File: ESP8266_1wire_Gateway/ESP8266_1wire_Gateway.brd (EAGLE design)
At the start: 44 x 44 mm, 72 parts, among them IC1 5V, IC2 3.3V, IC3 DS2482-100S, IC4 DS18B20, Q1 BSS84, Q2 BSS138, Q3 BSS138

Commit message: .
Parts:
- removed FLASH_SW: DTSM-3, mechanics:DTSM-3
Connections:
- net GND: no longer FLASH_SW.2
- net N$10: no longer FLASH_SW.1
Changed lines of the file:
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@@
 <element name="R14" library="resistor" package="R0805" value="4k7" x="11.1125" y="31.4325" rot="MR90"/>
 <element name="R13" library="resistor" package="R0805" value="4k7" x="14.2875" y="18.0975" rot="MR90"/>
-<element name="FLASH_SW" library="mechanics" package="DTSM-3" value="DTSM-3" x="26.7335" y="6.985" smashed="yes">
-<attribute name="NAME" x="24.1935" y="8.89" size="1.016" layer="25" ratio="14"/>
-</element>
 <element name="U$1" library="ohw-logo" package="OSHW_FILLX100_NOTEXT" value="" x="43.4275" y="34.5375" rot="MR0"/>
 <element name="IC2" library="SparkFun-PowerIC" package="SOT223" value="3.3V" x="21.082" y="18.7325" smashed="yes" rot="R180">
@@
 <contactref element="RESET" pad="1"/>
 <contactref element="C3" pad="2"/>
-<contactref element="FLASH_SW" pad="2"/>
 <contactref element="C6" pad="2"/>
 <contactref element="IC2" pad="1"/>
@@
 <wire x1="23.1762" y1="3.175" x2="20.32" y2="9.205" width="0" layer="19" extent="1-1"/>
 <wire x1="20.0025" y1="1.425" x2="23.1762" y2="3.175" width="0" layer="19" extent="1-1"/>
-<wire x1="30.2273" y1="6.985" x2="23.2397" y2="10.668" width="0" layer="19" extent="1-1"/>
-<wire x1="41.91" y1="9.525" x2="30.2273" y2="6.985" width="0" layer="19" extent="1-1"/>
-<wire x1="38.1" y1="7.62" x2="20.0025" y2="1.425" width="0" layer="19" extent="1-1"/>
+<wire x1="38.1" y1="7.62" x2="23.2397" y2="10.668" width="0" layer="19" extent="1-1"/>
+<wire x1="41.91" y1="9.525" x2="38.1" y2="7.62" width="0" layer="19" extent="1-1"/>
 </signal>
 <signal name="N$1">
@@
 <signal name="N$10">
 <contactref element="FLASH" pad="2"/>
-<contactref element="FLASH_SW" pad="1"/>
 <contactref element="R12" pad="1"/>
-<wire x1="13.0175" y1="9.21" x2="23.2397" y2="6.985" width="0" layer="19" extent="1-1"/>
-<wire x1="38.1" y1="10.16" x2="13.0175" y2="9.21" width="0" layer="19" extent="1-1"/>
+<wire x1="13.0175" y1="9.21" x2="38.1" y2="10.16" width="0" layer="19" extent="1-1"/>
 </signal>
 </signals>

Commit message: v0.9
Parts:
- removed CLR: (no value), my:1X02
- removed G12, G13: LSP10, my:LSP10
- added 1W1, 1W2: (no value), my:1X03
- added G4, G5: LSP10, my:LSP10
- added HSPI: (no value), my:1X04
- RST: value GND -> RST
- moved R1 33.5 mm to (36.2, 8.57)
- moved U$1 33.3 mm to (43.1, 1.20)
- moved U$2 33.3 mm to (40.3, 1.20)
- moved R3 32.2 mm to (28.6, 8.57)
- moved PF1 26.4 mm to (31.8, 25.7), turned to 0 degrees
- moved PRG 26.4 mm to (35.9, 31.4), turned to 180 degrees
- moved R14 26.0 mm to (23.5, 8.57), turned to 270 degrees
- moved R12 24.8 mm to (37.8, 8.26)
- moved R10 24.6 mm to (31.1, 8.57)
- moved C4 24.1 mm to (7.62, 36.5)
- moved SJ4 21.8 mm to (11.7, 32.1)
- moved SJ5 20.5 mm to (14.3, 32.1)
- moved R11 19.6 mm to (33.7, 8.57)
- moved R7 18.7 mm to (26.0, 8.57)
- moved SJ3 18.1 mm to (17.1, 32.1), turned to 90 degrees
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- renumbered GND8 to RST
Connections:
- net CSN renamed GPIO15
- removed net GPIO0: G0.1, MDL1.12, R12.2, R5.1
- removed net GPIO2: G2.1, MDL1.11, R4.1, SJ3.1
- new net 1WDIR: G0.1, MDL1.12, R12.2, R5.1, SJ3.1
- new net GPIO5: G5.1, MDL1.14, R8.1
- new net HCS0: HSPI.4, MDL1.17
- new net HMISO: HSPI.3, MDL1.18
- new net HMOSI: HSPI.2, MDL1.21
- new net HSCLK: HSPI.1, MDL1.22
- net 1W_ESD: now also 1W1.2, 1W2.2
- net GND: no longer RST.1
- net GND_ESD: now also 1W1.3, 1W2.3
- net LED_OPT: now also G4.1, MDL1.13, R9.1; no longer G12.1, MDL1.6, R8.1
- net RST: now also RST.1
- net RXD: no longer CLR.2
- net SCL1: now also MDL1.6; no longer MDL1.14
- net SDA1: now also MDL1.7; no longer MDL1.13
- net SW_OPT: now also G2.1, MDL1.11, R4.1; no longer G13.1, MDL1.7, R9.1
- net TXD: no longer CLR.1
- net VCC_5V: now also 1W1.1, 1W2.1
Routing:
- net GND: track 0.00 -> 204.1 mm, vias 0 -> 3
- net VCC: track 0.00 -> 128.6 mm, vias 0 -> 2
- net VCC_5V: track 0.00 -> 89.1 mm, vias 0 -> 3
- net 5V_IN: track 0.00 -> 86.9 mm, vias 0 -> 2
- net LED_OPT: track 0.00 -> 86.1 mm, vias 0 -> 3
- net SW_OPT: track 0.00 -> 84.2 mm, vias 0 -> 3
- net 1WDIR: track 0.00 -> 80.2 mm, vias 0 -> 2
- net SCL1: track 0.00 -> 70.3 mm, vias 0 -> 2
- net RST: track 0.00 -> 63.4 mm, vias 0 -> 1
- net SDA2: track 0.00 -> 60.4 mm, vias 0 -> 1
- net GPIO15: track 0.00 -> 59.7 mm
- net N$5: track 0.00 -> 58.7 mm
- net SDA1X: track 0.00 -> 56.3 mm, vias 0 -> 1
- net CH_PD: track 0.00 -> 52.5 mm, vias 0 -> 2
- net GPIO5: track 0.00 -> 47.9 mm, vias 0 -> 2
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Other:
- board text added: "CS0"
- board text added: "EXT"
- board text added: "MISO"
- board text added: "MOSI"
- board text added: "RST"
- board text added: "RXD"
- board text added: "SCLK"
- board text added: "TXD"

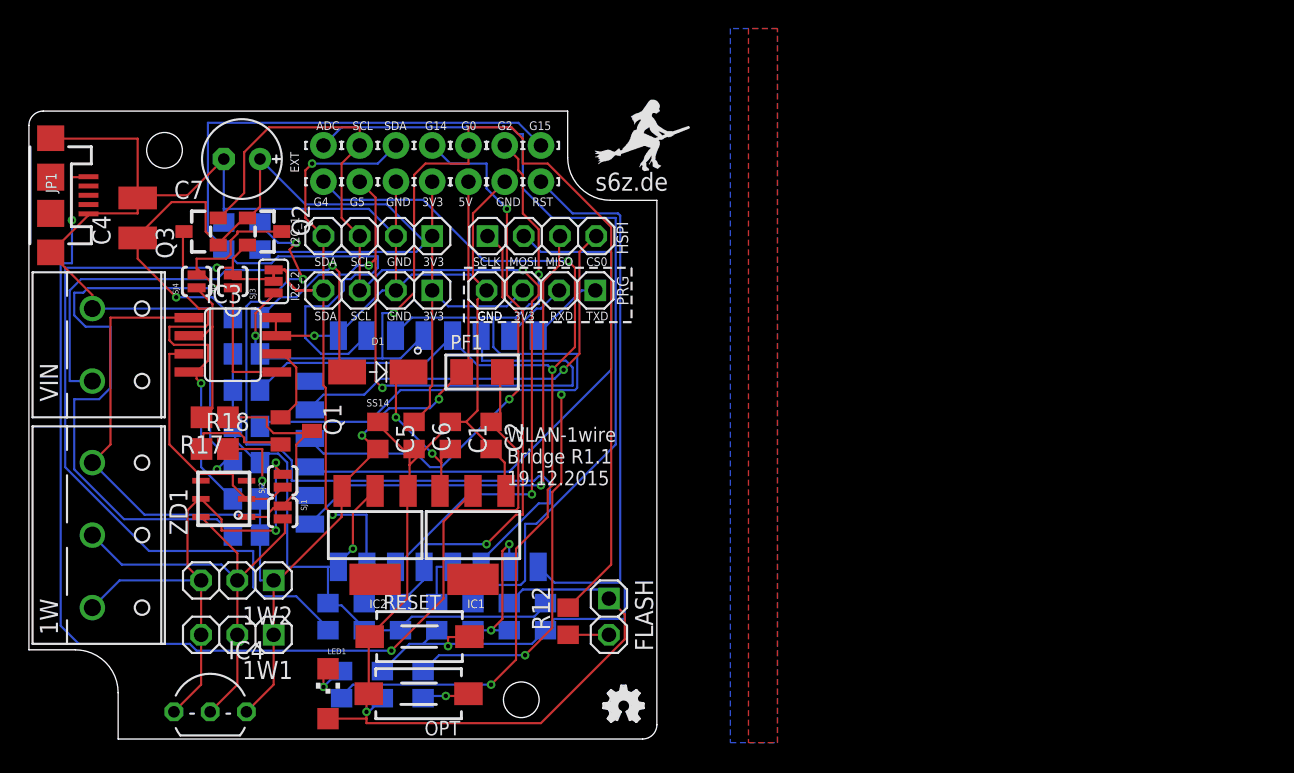
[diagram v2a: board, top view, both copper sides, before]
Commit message: Version 1.2 : ELKO / THT Version 1.3 : tantal / SMD
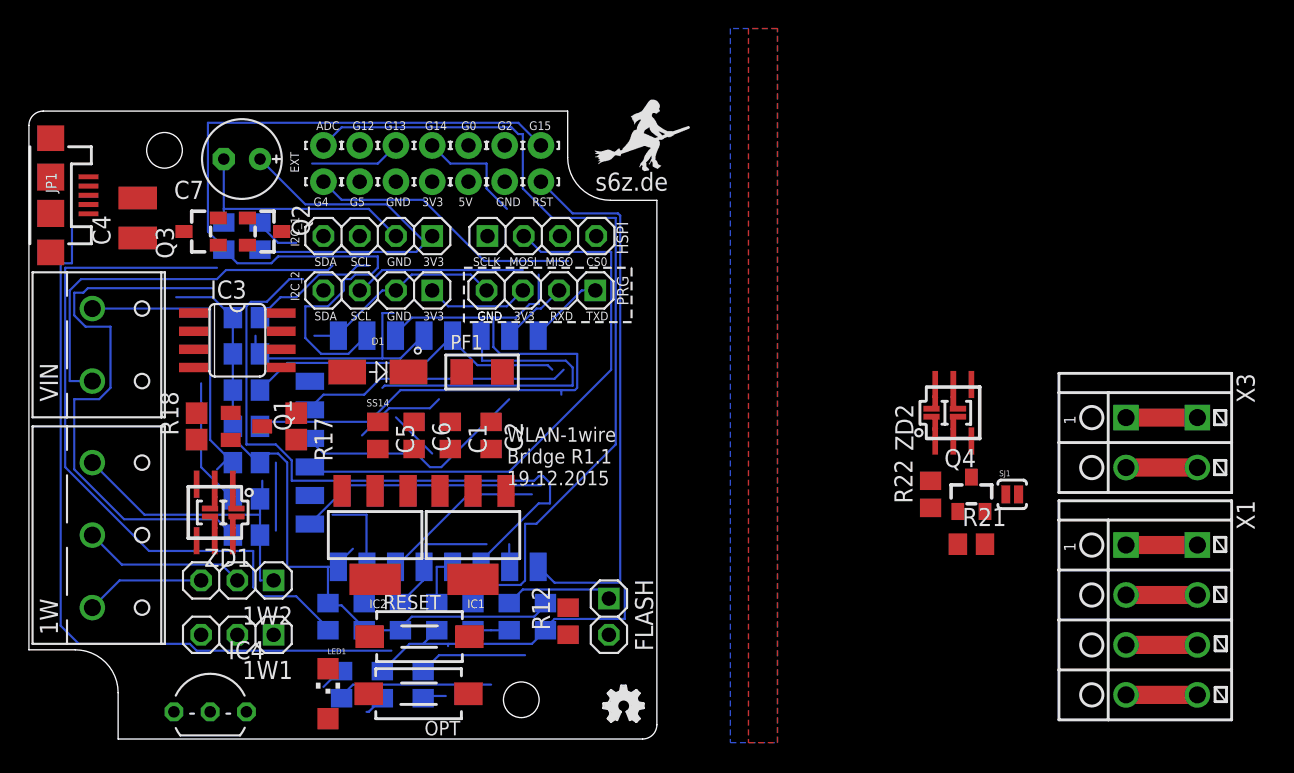
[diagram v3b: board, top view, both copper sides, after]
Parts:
- removed SJ2, SJ4, SJ5: JUMPER-PAD-2-NOYES_SILK, SparkFun-Passives:PAD-JUMPER-2-NO_YES_SILK
- removed SJ3: JUMPER-PAD-3-2OF3_NC_BY_TRACE_SMALL, SparkFun-Passives:PAD-JUMPER-3-2OF3_NC_BY_TRACE_YES_SILK_FULL_BOX
- added Q4: BSS138, my:SOT23
- added R21, R22: 10k, resistor:R0805
- added X1: (no value), my:CON_350-104
- added X3: (no value), my:CON_350-102
- added ZD2: DS9503_BYPASS_JP, my:TSOC6_BYPASS_J
- ZD1: value DS9503P -> DS9503_BYPASS_JP; device 1wire:TSOC6 -> my:TSOC6_BYPASS_J
- moved SJ1 51.1 mm to (68.9, 17.1), turned to 0 degrees
- moved R17 5.75 mm to (18.7, 21.9), turned to 270 degrees
- moved Q1 3.51 mm to (15.2, 21.9)
- moved R18 2.03 mm to (11.7, 21.9), turned to 90 degrees
- moved ZD1 1.14 mm to (13.0, 15.9), turned to 180 degrees
- moved IC3 0.45 mm to (14.6, 27.9)
- renumbered SCL to G12, SDA to G13
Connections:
- removed net GPIO5: G5.1, MDL1.14, R8.1
- removed net SDA1X: Q2.2, R13.1, SJ3.2, SJ5.2
- new net 1WD_ESD: ZD2.6
- new net 1W_1: Q4.3, R22.2, SJ1.1, ZD2.1
- new net GNDD_ESD: ZD2.5
- new net GPIO13: G13.1, MDL1.7
- net 1W: no longer SJ4.1
- net 1WDIR: now also Q4.2, R21.2, SJ1.2; no longer SJ3.1
- net 1W_: no longer SJ1.1
- net 1W_ESD: no longer SJ1.2
- net GND: now also ZD2.2; no longer SJ2.1
- net GND_ESD: no longer SJ2.2
- net LED_OPT: now also G12.1, MDL1.6; no longer G4.1, MDL1.13, R9.1
- net SCL1: now also G5.1, MDL1.14, R8.1; no longer G12.1, MDL1.6
- net SDA1: now also G4.1, MDL1.13, Q2.2, R13.1, R9.1; no longer G13.1, MDL1.7, SJ3.3
- net SDA2: no longer SJ4.2, SJ5.1
- net VCC: now also Q4.1, R21.1
- net VCC_5V: now also R22.1
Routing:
- net GND: track 204.1 -> 62.1 mm, vias 3 -> 0
- net LED_OPT: track 86.1 -> 22.6 mm, vias 3 -> 0
- net 1WDIR: track 80.2 -> 17.8 mm, vias 2 -> 0
- net VCC_5V: track 89.1 -> 27.8 mm, vias 3 -> 0
- net SDA1X: track 56.3 -> 0.00 mm, vias 1 -> 0
- net SDA1: track 42.5 -> 92.2 mm, vias 2 -> 0
- net GPIO5: track 47.9 -> 0.00 mm, vias 2 -> 0
- net VCC: track 128.6 -> 84.5 mm, vias 2 -> 0
- net 5V_IN: track 86.9 -> 53.9 mm, vias 2 -> 0
- net SW_OPT: track 84.2 -> 54.9 mm, vias 3 -> 0
- net GPIO14: track 42.6 -> 17.3 mm, vias 2 -> 0
- net GND_ESD: track 37.4 -> 13.2 mm, vias 2 -> 0
- net SCL1: track 70.3 -> 47.6 mm, vias 2 -> 0
- net 1W_ESD: track 32.7 -> 11.5 mm
- net SDA2: track 60.4 -> 39.4 mm, vias 1 -> 0
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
